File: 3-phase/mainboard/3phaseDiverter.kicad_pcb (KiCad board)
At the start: 2 copper layers, 144.8 x 120.6 mm, 98 parts, among them CN9 SMA, IC1 ATmega328-P, IC2 LM358, J0 FTDI, J1 RESET, J10 D10, J11 D11, J12 D12, J13 D13, J14 +5V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

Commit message: Tuning
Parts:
- removed kibuzzard-62501737: G***, kibuzzard-62501737
- removed kibuzzard-625018AA: G***, kibuzzard-625018AA
- removed kibuzzard-625018BF: G***, kibuzzard-625018BF
- removed kibuzzard-6341D348: G***, kibuzzard-6341D348
- added kibuzzard-6431E2C3: G***, kibuzzard-6431E2C3, F.Cu at (17.3, 77.2)
- added kibuzzard-6431E73F: G***, kibuzzard-6431E73F, F.Cu at (39.1, 121.9)
- added kibuzzard-6431E749: G***, kibuzzard-6431E749, F.Cu at (87.3, 121.9)
- added kibuzzard-6431E750: G***, kibuzzard-6431E750, F.Cu at (135.8, 121.9)
- REF** (x2): value MountingHole_4.3mm_M4_DIN965 -> MountingHole_4.3mm_M4_ISO14580_Pad_TopBottom; footprint MountingHole:MountingHole_4.3mm_M4_DIN965 -> MountingHole:MountingHole_4.3mm_M4_ISO14580_Pad_TopBottom
- moved C12 6.29 mm to (143.0, 66.8), turned to -90 degrees
- moved C11 4.95 mm to (141.8, 62.6)
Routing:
- net +5V: track 39.6 -> 40.4 mm
- net GND: vias 82 -> 85

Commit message: Upt pcb
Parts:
- removed kibuzzard-6431E2C3: G***, kibuzzard-6431E2C3
- added kibuzzard-64A48EB5: G***, kibuzzard-64A48EB5, F.Cu at (17.3, 77.2)
- CT1, CT2, CT3, J1, J14, J15, J20, J30: footprint UserDef:Molex_SL_171971-0002_1x02_P2.54mm_Vertical -> Library:Molex_SL_171971-0002_1x02_P2.54mm_Vertical
- J0: footprint UserDef:Molex_SL_171971-0006_1x06_P2.54mm_Vertical -> Library:Molex_SL_171971-0006_1x06_P2.54mm_Vertical
- J10, J11, J12, J13, J2, J3, J4, J5, J6, J7, J8, J9: footprint UserDef:Molex_SL_171971-0003_1x03_P2.54mm_Vertical -> Library:Molex_SL_171971-0003_1x03_P2.54mm_Vertical
- JP1, JP2: footprint UserDef:SolderWire-0.75sqmm_1x02_P5.08mm_D1.25mm_OD2.3mm -> Library:SolderWire-0.75sqmm_1x02_P5.08mm_D1.25mm_OD2.3mm
- TXFR1, TXFR2, TXFR3: footprint Transformer_THT:Transformer_Myrra_44163 -> Library:Transformer_Myrra_44163
- moved C2 1.29 mm to (140.4, 32.8)
- moved C4 1.16 mm to (139.9, 38.6)
- moved J30 1.16 mm to (142.4, 45.9)
- moved J20 1.09 mm to (156.0, 23.5)
- moved VR1 0.51 mm to (145.5, 22.2)
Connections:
- REF** pad 1: Earth -> (no net)
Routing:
- net VCC: track 268.9 -> 270.2 mm

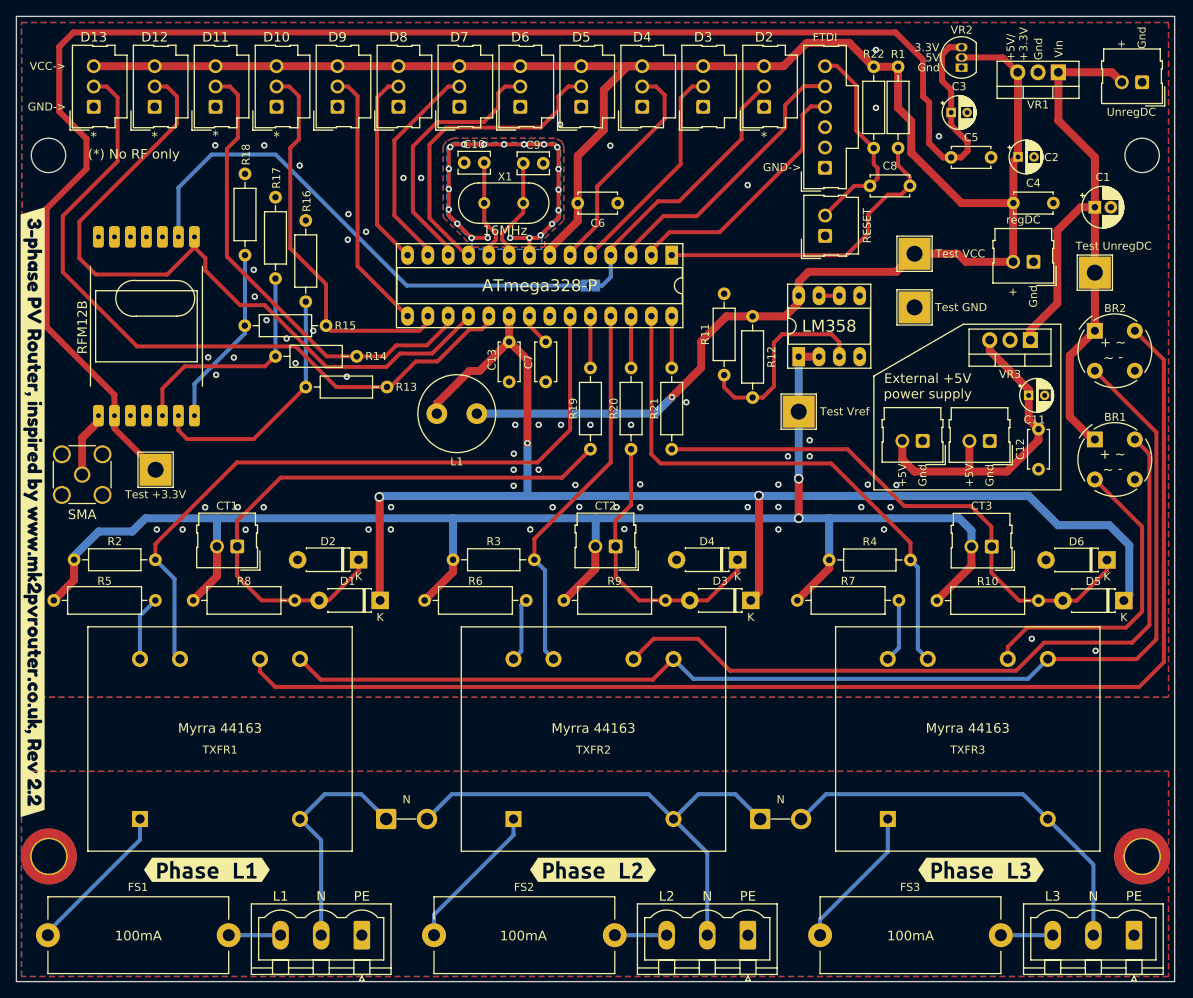
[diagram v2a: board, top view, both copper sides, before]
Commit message: Update some footprint
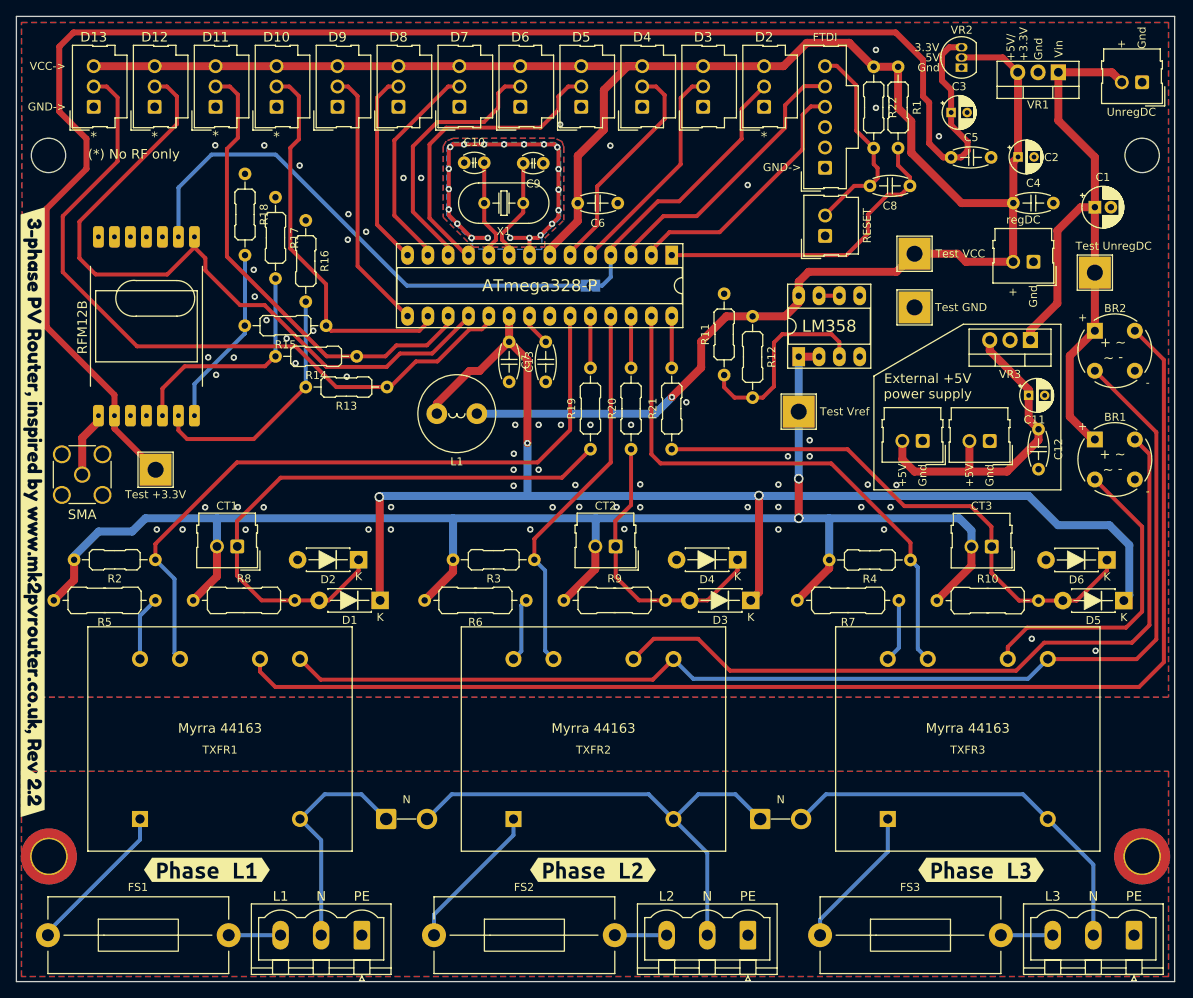
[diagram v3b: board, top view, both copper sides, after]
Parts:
- BR1, BR2: footprint Diode_THT:Diode_Bridge_Round_D9.0mm -> PCM_Diode_THT_AKL:Diode_Bridge_Round_D9.0mm
- C10, C9: footprint Capacitor_THT:C_Disc_D3.8mm_W2.6mm_P2.50mm -> PCM_Capacitor_THT_AKL:C_Disc_D3.8mm_W2.6mm_P2.50mm
- C12, C13, C4, C5, C6, C7, C8: footprint Capacitor_THT:C_Disc_D4.7mm_W2.5mm_P5.00mm -> PCM_Capacitor_THT_AKL:C_Disc_D4.7mm_W2.5mm_P5.00mm
- D1, D2, D3, D4, D5, D6: footprint Diode_THT:D_DO-41_SOD81_P7.62mm_Horizontal -> PCM_Diode_THT_AKL:D_DO-41_SOD81_P7.62mm_Horizontal
- FS1, FS2, FS3: footprint Fuse:Fuseholder_Cylinder-5x20mm_Stelvio-Kontek_PTF78_Horizontal_Open -> PCM_Fuse_AKL:Fuseholder_Cylinder-5x20mm_Stelvio-Kontek_PTF78_Horizontal_Open
- L1: footprint Inductor_THT:L_Radial_D9.5mm_P5.00mm_Fastron_07HVP -> PCM_Inductor_THT_AKL:L_Radial_D9.5mm_P5.00mm_Fastron_07HVP
- R1, R11, R12, R13, R14, R15, R16, R17, R18, R19, R2, R20, R21, R22, R3, R4: footprint Resistor_THT:R_Axial_DIN0207_L6.3mm_D2.5mm_P10.16mm_Horizontal -> PCM_Resistor_THT_AKL:R_Axial_DIN0207_L6.3mm_D2.5mm_P10.16mm_Horizontal
- R10, R5, R6, R7, R8, R9: footprint Resistor_THT:R_Axial_DIN0309_L9.0mm_D3.2mm_P12.70mm_Horizontal -> PCM_Resistor_THT_AKL:R_Axial_DIN0309_L9.0mm_D3.2mm_P12.70mm_Horizontal
- X1: footprint Crystal:Crystal_HC49-U_Vertical -> PCM_Crystal_AKL:Crystal_HC49-U_Vertical

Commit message: V3.0
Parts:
- removed kibuzzard-64A48EB5: G***, kibuzzard-64A48EB5
- added BR3: B40R, PCM_Diode_THT_AKL:Diode_Bridge_Round_D9.0mm, F.Cu at (156.5, 99.2)
- added kibuzzard-64C01F08: G***, kibuzzard-64C01F08, F.Cu at (17.3, 77.2)
- moved BR1 89.8 mm to (65.8, 99.2), turned to 180 degrees
- moved BR2 59.2 mm to (111.2, 99.2), turned to 180 degrees
- moved J20 25.2 mm to (155.6, 48.7)
- moved TP0 25.2 mm to (155.2, 71.9)
- moved C11 5.36 mm to (146.7, 64.7)
- moved C12 5.04 mm to (147.9, 68.2)
- moved J14 4.88 mm to (133.4, 68.3)
- moved J15 4.88 mm to (141.8, 68.3)
- moved VR1 3.35 mm to (148.8, 22.2)
- moved TXFR3 2.73 mm to (121.4, 115.7)
- moved JP2 2.03 mm to (106.3, 115.5)
- moved TXFR2 1.30 mm to (76.1, 115.6)
- moved JP1 0.71 mm to (60.9, 115.6)
- moved VR3 0.43 mm to (142.3, 55.4)
- moved C1 0.06 mm to (150.1, 39.1)
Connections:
- TXFR1 pad 6: Net-(BR2-Pad2) -> Net-(BR1-Pad2)
- TXFR1 pad 7: Net-(BR2-Pad4) -> Net-(BR1-Pad4)
- TXFR2 pad 7: Net-(BR1-Pad4) -> Net-(BR2-Pad4)
- TXFR3 pad 6: Net-(BR2-Pad2) -> Net-(BR3-Pad2)
- TXFR3 pad 7: Net-(BR1-Pad2) -> Net-(BR3-Pad4)
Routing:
- net Net-(BR2-Pad4): track 159.6 -> 16.7 mm
- net Net-(BR2-Pad2): track 149.0 -> 16.6 mm
- net UnregDC+: track 79.7 -> 195.9 mm
- net Net-(BR1-Pad4): track 93.5 -> 16.7 mm
- net Net-(BR1-Pad2): track 39.1 -> 16.5 mm
- net Net-(BR3-Pad4): track 0.00 -> 16.6 mm
- net Net-(BR3-Pad2): track 0.00 -> 16.5 mm
- net +5V: track 40.4 -> 48.1 mm
- net VCC: track 270.2 -> 274.9 mm
- net Net-(JP1-A): track 29.0 -> 25.7 mm
- net Net-(JP1-B): track 63.1 -> 60.8 mm
- net Net-(R7-Pad1): track 7.90 -> 9.15 mm
- net Net-(FS3-Pad1): track 18.0 -> 16.8 mm
- net Net-(JP2-B): track 50.3 -> 51.5 mm
- net GND: vias 85 -> 84
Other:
- outline, holes or cut-outs redrawn
- board text removed: "- ~ ~ +"

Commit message: Tuning
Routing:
- net GND: vias 84 -> 180
- net Earth: vias 0 -> 9

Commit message: PCB tuning
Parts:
- added G***: LOGO, LOGO, F.Cu at (54.0, 71.5)
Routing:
- net GND: vias 180 -> 185
